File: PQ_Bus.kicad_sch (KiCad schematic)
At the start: 11 parts, among them J1 PQ9-Connector, U6 TCAN334

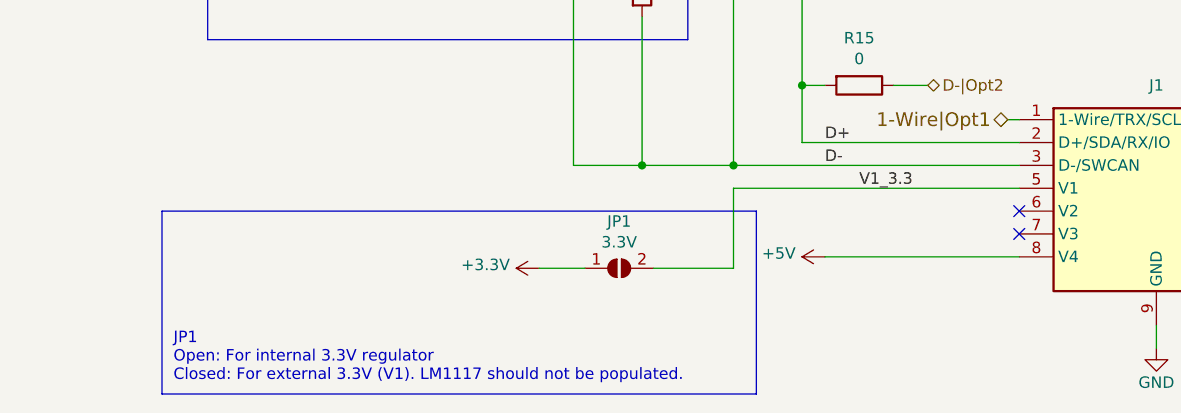
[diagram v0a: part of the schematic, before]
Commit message: Add I2C multiplexer
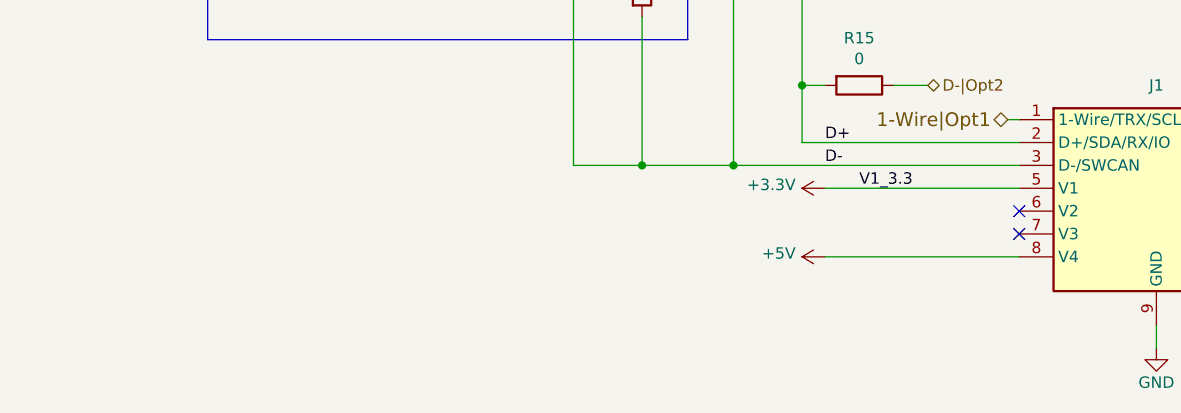
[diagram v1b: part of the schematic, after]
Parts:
- removed JP1: 3.3V, Jumper:SolderJumper-2_P1.3mm_Open_Pad1.0x1.5mm, symbol Jumper:SolderJumper_2_Open
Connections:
- net V1_3.3 is gone; now on net +3V3: J1.5 (V1)
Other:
- note removed: "JP1 Open: For internal 3.3V regulator Closed: For external 3.3V (V1). LM1117 should not be populated."
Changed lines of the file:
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@@
     (stroke (width 0) (type default))
   )
-  (wire (pts (xy 190.5 127) (xy 222.25 127))
+  (wire (pts (xy 200.66 127) (xy 222.25 127))
     (stroke (width 0) (type default))
   )
@@
     (stroke (width 0) (type default))
   )
-  (polyline (pts (xy 193.04 129.54) (xy 193.04 149.86))
-    (stroke (width 0) (type default))
-  )
   (wire (pts (xy 119.38 71.12) (xy 129.54 71.12))
     (stroke (width 0) (type default))
@@
     (stroke (width 0) (type default))
   )
-  (polyline (pts (xy 127 149.86) (xy 127 129.54))
-    (stroke (width 0) (type default))
-  )
   (wire (pts (xy 180.34 107.95) (xy 180.34 124.46))
     (stroke (width 0) (type default))
@@
     (stroke (width 0) (type default))
   )
-  (wire (pts (xy 173.99 135.89) (xy 168.91 135.89))
-    (stroke (width 0) (type default))
-  )
   (wire (pts (xy 119.38 73.66) (xy 153.67 73.66))
     (stroke (width 0) (type default))
@@
     (stroke (width 0) (type default))
   )
-  (polyline (pts (xy 193.04 149.86) (xy 127 149.86))
-    (stroke (width 0) (type default))
-  )
-  (wire (pts (xy 190.5 135.89) (xy 190.5 127))
-    (stroke (width 0) (type default))
-  )
   (wire (pts (xy 137.16 66.04) (xy 153.67 66.04))
     (stroke (width 0) (type default))
@@
     (stroke (width 0) (type default))
   )
-  (polyline (pts (xy 127 129.54) (xy 193.04 129.54))
-    (stroke (width 0) (type default))
-  )
   (wire (pts (xy 198.12 66.04) (xy 198.12 99.06))
     (stroke (width 0) (type default))
@@
   (wire (pts (xy 172.72 124.46) (xy 180.34 124.46))
     (stroke (width 0) (type default))
-  )
-  (wire (pts (xy 181.61 135.89) (xy 190.5 135.89))
-    (stroke (width 0) (type default))
-  )
-  (text "JP1\nOpen: For internal 3.3V regulator\nClosed: For external 3.3V (V1). LM1117 should not be populated."
-    (at 128.27 148.59 0)
-    (effects (font (size 1.27 1.27)) (justify left bottom))
   )
   (text "Driverless CAN" (at 168.91 86.36 0)
@@
     )
   )
-  (symbol (lib_id "Jumper:SolderJumper_2_Open") (at 177.8 135.89 0) (unit 1)
-    (in_bom no) (on_board yes) (dnp no)
-    (property "Reference" "JP1" (at 177.8 130.683 0)
-      (effects (font (size 1.27 1.27)))
-    )
-    (property "Value" "3.3V" (at 177.8 132.9944 0)
-      (effects (font (size 1.27 1.27)))
-    )
-    (property "Footprint" "Jumper:SolderJumper-2_P1.3mm_Open_Pad1.0x1.5mm" (at 177.8 135.89 0)
-      (effects (font (size 1.27 1.27)) hide)
-    )
-    (property "Datasheet" "~" (at 177.8 135.89 0)
-      (effects (font (size 1.27 1.27)) hide)
-    )
-    (pin "1")
-    (pin "2")
-    (instances
-      (project "NEW_PCB_ADCS"
-        (path "/42c40d7d-71af-4ce9-bac9-d638f259c957/00000000-0000-0000-0000-00005a289551"
-          (reference "JP1") (unit 1)
-        )
-      )
-      (project "pq9ish-main-hw"
-        (path "/619b49ed-1bcd-4c84-8c0f-98372f01728f/00000000-0000-0000-0000-00005a289551"
-          (reference "JP1") (unit 1)
-        )
-      )
-    )
-  )
   (symbol (lib_id "power:+5V") (at 200.66 134.62 90) (unit 1)
     (in_bom yes) (on_board yes) (dnp no)
@@
     )
   )
-  (symbol (lib_id "power:+3.3V") (at 168.91 135.89 90) (unit 1)
-    (in_bom yes) (on_board yes) (dnp no)
-    (property "Reference" "#PWR0102" (at 172.72 135.89 0)
-      (effects (font (size 1.27 1.27)) hide)
-    )
-    (property "Value" "+3.3V" (at 165.6588 135.509 90)
-      (effects (font (size 1.27 1.27)) (justify left))
-    )
-    (property "Footprint" "" (at 168.91 135.89 0)
-      (effects (font (size 1.27 1.27)) hide)
-    )
-    (property "Datasheet" "" (at 168.91 135.89 0)
-      (effects (font (size 1.27 1.27)) hide)
-    )
+  (symbol (lib_id "power:+3.3V") (at 200.66 127 90) (unit 1)
+    (in_bom yes) (on_board yes) (dnp no)
+    (property "Reference" "#PWR0102" (at 204.47 127 0)
+      (effects (font (size 1.27 1.27)) hide)
+    )
+    (property "Value" "+3.3V" (at 197.4088 126.619 90)
+      (effects (font (size 1.27 1.27)) (justify left))
+    )
+    (property "Footprint" "" (at 200.66 127 0)
+      (effects (font (size 1.27 1.27)) hide)
+    )
+    (property "Datasheet" "" (at 200.66 127 0)
+      (effects (font (size 1.27 1.27)) hide)
+    )

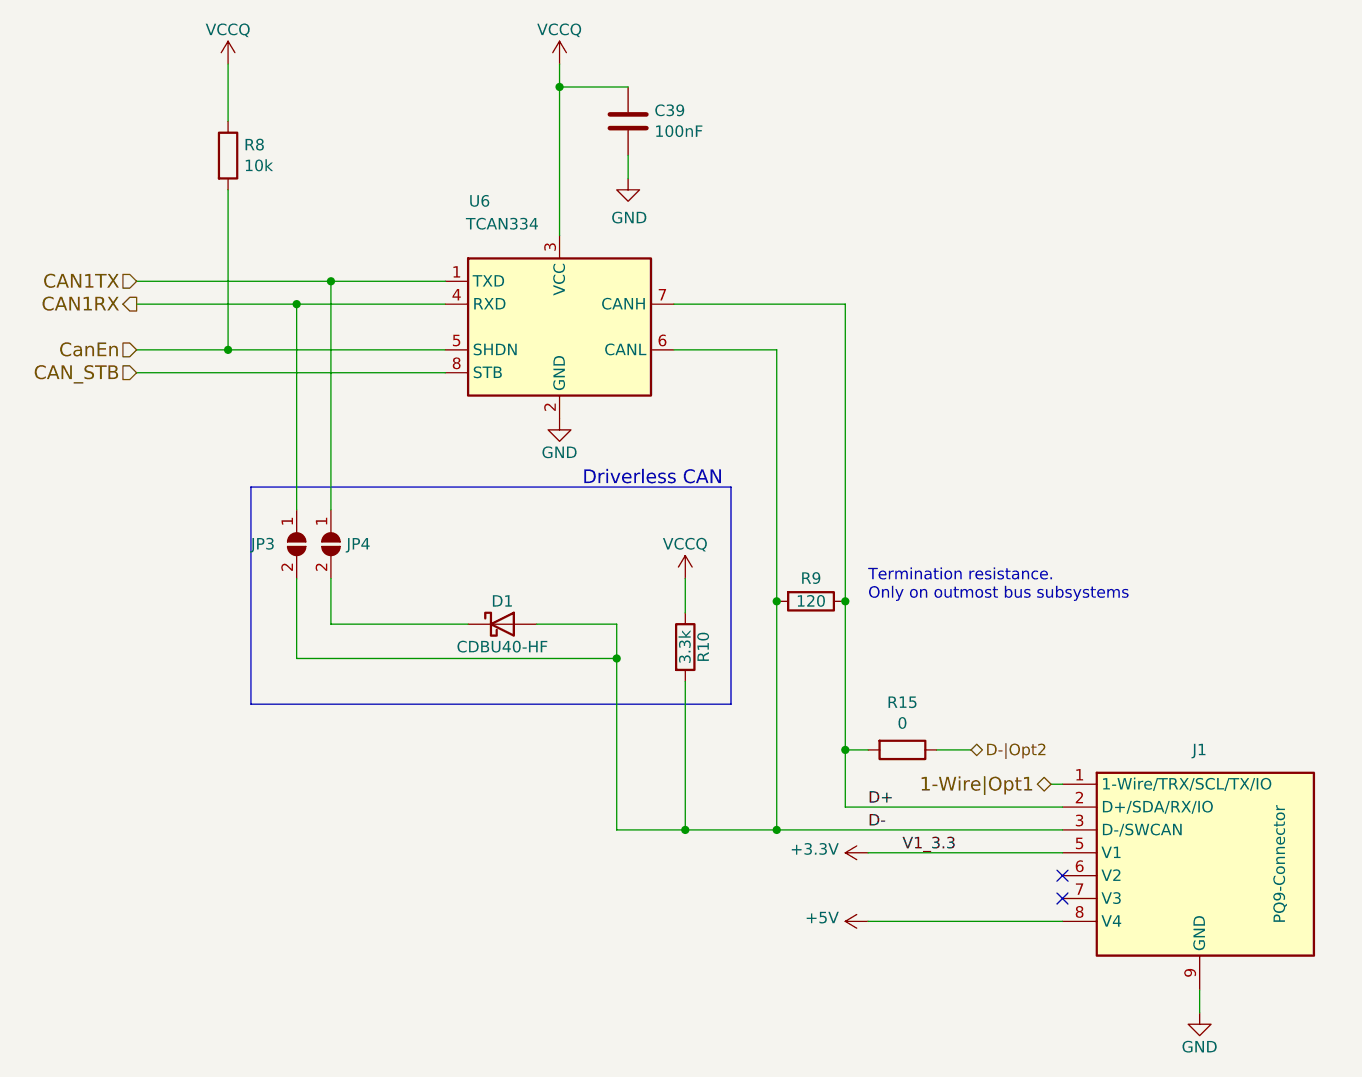
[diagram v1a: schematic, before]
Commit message: Reannotate schematic
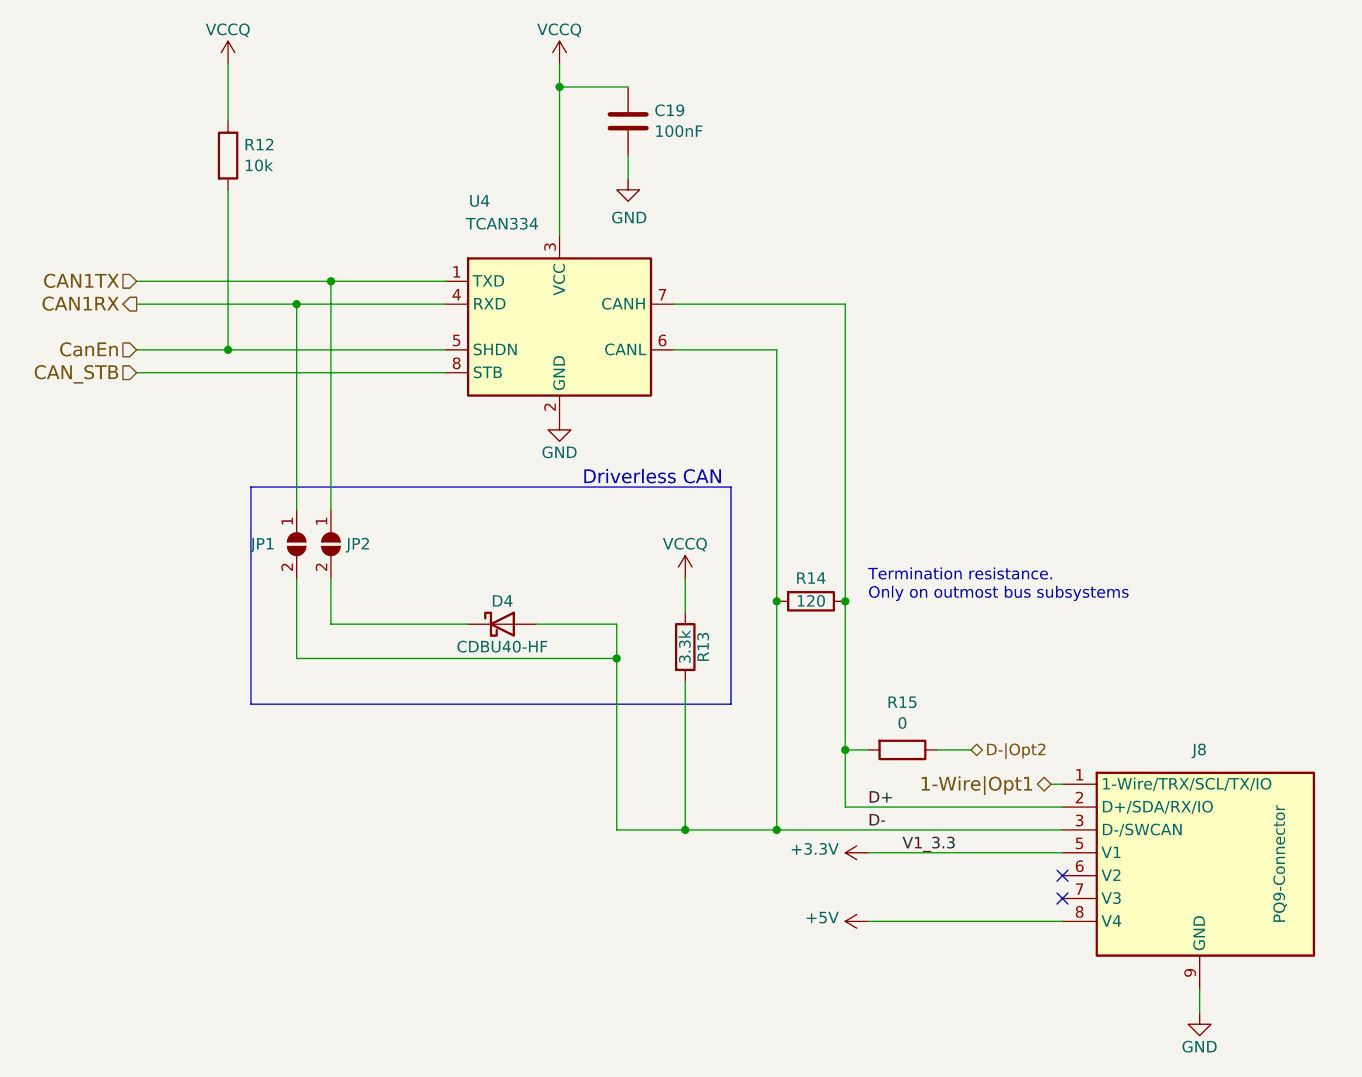
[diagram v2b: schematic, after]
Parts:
- renumbered C39 to C19, D1 to D4, J1 to J8, JP3 to JP1, JP4 to JP2, R8 to R12, R10 to R13, R9 to R14, U6 to U4

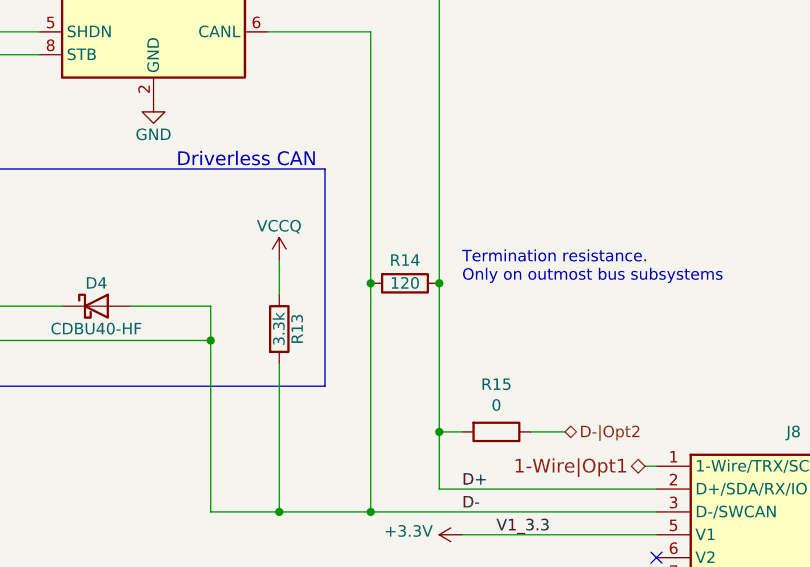
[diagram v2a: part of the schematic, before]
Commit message: Create PCB layout and routing
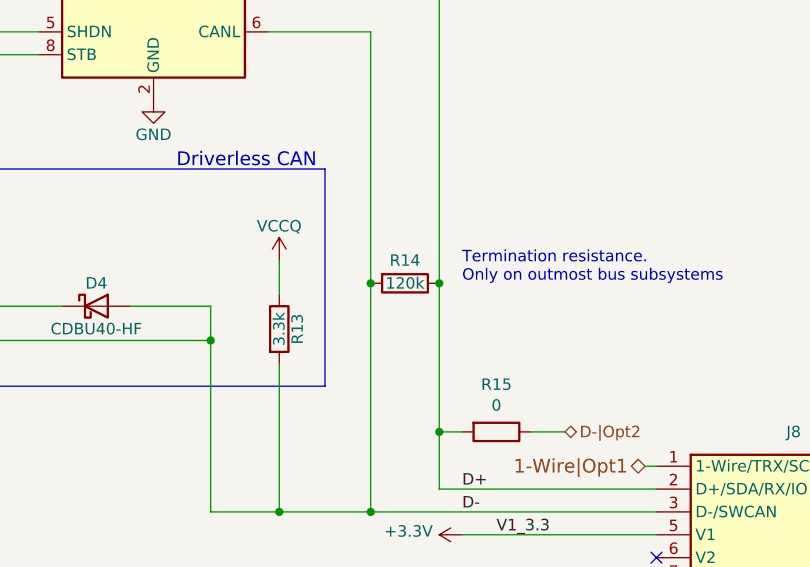
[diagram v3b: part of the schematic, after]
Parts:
- R12, R13, R15: footprint Resistor_SMD:R_0603_1608Metric_Pad1.05x0.95mm_HandSolder -> Resistor_SMD:R_0603_1608Metric
- R14: value 120 -> 120k; footprint Resistor_SMD:R_0603_1608Metric_Pad1.05x0.95mm_HandSolder -> Resistor_SMD:R_0603_1608Metric
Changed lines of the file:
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@@
       (effects (font (size 1.27 1.27)))
     )
-    (property "Footprint" "Resistor_SMD:R_0603_1608Metric_Pad1.05x0.95mm_HandSolder" (at 178.562 104.14 90)
+    (property "Footprint" "Resistor_SMD:R_0603_1608Metric" (at 178.562 104.14 90)
       (effects (font (size 1.27 1.27)) hide)
     )
@@
       (effects (font (size 1.27 1.27)))
     )
-    (property "Value" "120" (at 194.31 99.06 90)
-      (effects (font (size 1.27 1.27)))
-    )
-    (property "Footprint" "Resistor_SMD:R_0603_1608Metric_Pad1.05x0.95mm_HandSolder" (at 194.31 97.282 90)
+    (property "Value" "120k" (at 194.31 99.06 90)
+      (effects (font (size 1.27 1.27)))
+    )
+    (property "Footprint" "Resistor_SMD:R_0603_1608Metric" (at 194.31 97.282 90)
       (effects (font (size 1.27 1.27)) hide)
     )
@@
       (effects (font (size 1.27 1.27)) (justify left))
     )
-    (property "Footprint" "Resistor_SMD:R_0603_1608Metric_Pad1.05x0.95mm_HandSolder" (at 127.762 49.53 90)
+    (property "Footprint" "Resistor_SMD:R_0603_1608Metric" (at 127.762 49.53 90)
       (effects (font (size 1.27 1.27)) hide)
     )
@@
       (effects (font (size 1.27 1.27)))
     )
-    (property "Footprint" "Resistor_SMD:R_0603_1608Metric_Pad1.05x0.95mm_HandSolder" (at 204.47 113.792 90)
-      (effects (font (size 1.27 1.27)) hide)
-    )
+    (property "Footprint" "Resistor_SMD:R_0603_1608Metric" (at 204.47 113.792 90)
+      (effects (font (size 1.27 1.27)) hide)
+    )

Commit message: Fix some issues
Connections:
- net +3V3 renamed +3.3VP
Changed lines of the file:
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@@
-    (effects (font (size 1.27 1.27)) (justify left bottom))
-  )
-  (label "V1_3.3" (at 204.47 127 0) (fields_autoplaced)
     (effects (font (size 1.27 1.27)) (justify left bottom))
   )
@@
     )
   )
-  (symbol (lib_id "power:+3.3V") (at 200.66 127 90) (unit 1)
-    (in_bom yes) (on_board yes) (dnp no)
-    (property "Reference" "#PWR060" (at 204.47 127 0)
-      (effects (font (size 1.27 1.27)) hide)
-    )
-    (property "Value" "+3.3V" (at 197.4088 126.619 90)
+  (symbol (lib_id "Device:R") (at 204.47 115.57 270) (unit 1)
+    (in_bom yes) (on_board yes) (dnp no)
+    (property "Reference" "R15" (at 204.47 110.3122 90)
+      (effects (font (size 1.27 1.27)))
+    )
+    (property "Value" "0" (at 204.47 112.6236 90)
+      (effects (font (size 1.27 1.27)))
+    )
+    (property "Footprint" "Resistor_SMD:R_0603_1608Metric" (at 204.47 113.792 90)
+      (effects (font (size 1.27 1.27)) hide)
+    )
+    (property "Datasheet" "~" (at 204.47 115.57 0)
+      (effects (font (size 1.27 1.27)) hide)
+    )
+    (property "Variant" "PQBus Opt-2" (at 204.47 115.57 90)
+      (effects (font (size 1.27 1.27)) hide)
+    )
+    (pin "1")
+    (pin "2")
+    (instances
+      (project "NEW_PCB_ADCS"
+        (path "/42c40d7d-71af-4ce9-bac9-d638f259c957/00000000-0000-0000-0000-00005a289551"
+          (reference "R15") (unit 1)
+        )
+      )
+      (project "pq9ish-main-hw"
+        (path "/619b49ed-1bcd-4c84-8c0f-98372f01728f/00000000-0000-0000-0000-00005a289551"
+          (reference "R15") (unit 1)
+        )
+      )
+    )
+  )
+  (symbol (lib_id "power:+3.3VP") (at 200.66 127 90) (unit 1)
+    (in_bom yes) (on_board yes) (dnp no) (fields_autoplaced)
+    (property "Reference" "#PWR060" (at 201.93 123.19 0)
+      (effects (font (size 1.27 1.27)) hide)
+    )
+    (property "Value" "+3.3VP" (at 196.85 127.635 90)
       (effects (font (size 1.27 1.27)) (justify left))
     )
@@
         )
       )
-      (project "pq9ish-main-hw"
-        (path "/619b49ed-1bcd-4c84-8c0f-98372f01728f/00000000-0000-0000-0000-00005a289551"
-          (reference "#PWR0102") (unit 1)
-        )
-      )
-    )
-  )
-  (symbol (lib_id "Device:R") (at 204.47 115.57 270) (unit 1)
-    (in_bom yes) (on_board yes) (dnp no)
-    (property "Reference" "R15" (at 204.47 110.3122 90)
-      (effects (font (size 1.27 1.27)))
-    )
-    (property "Value" "0" (at 204.47 112.6236 90)
-      (effects (font (size 1.27 1.27)))
-    )
-    (property "Footprint" "Resistor_SMD:R_0603_1608Metric" (at 204.47 113.792 90)
-      (effects (font (size 1.27 1.27)) hide)
-    )
-    (property "Datasheet" "~" (at 204.47 115.57 0)
-      (effects (font (size 1.27 1.27)) hide)
-    )
-    (property "Variant" "PQBus Opt-2" (at 204.47 115.57 90)
-      (effects (font (size 1.27 1.27)) hide)
-    )
-    (pin "1")
-    (pin "2")
-    (instances
-      (project "NEW_PCB_ADCS"
-        (path "/42c40d7d-71af-4ce9-bac9-d638f259c957/00000000-0000-0000-0000-00005a289551"
-          (reference "R15") (unit 1)
-        )
-      )
-      (project "pq9ish-main-hw"
-        (path "/619b49ed-1bcd-4c84-8c0f-98372f01728f/00000000-0000-0000-0000-00005a289551"
-          (reference "R15") (unit 1)
-        )
-      )

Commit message: Update some part numbers
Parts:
- R12: MPN (none) -> RE0603BRE0710KL
- R15: Part Number (none) -> RMCF0603ZT0R00
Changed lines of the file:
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@@
+      (effects (font (size 1.27 1.27)) hide)
+    )
+    (property "MPN" "RE0603BRE0710KL" (at 129.54 49.53 0)
       (effects (font (size 1.27 1.27)) hide)
     )
@@
       (effects (font (size 1.27 1.27)) hide)
     )
+    (property "Part Number" "RMCF0603ZT0R00" (at 204.47 115.57 0)
+      (effects (font (size 1.27 1.27)) hide)
+    )
